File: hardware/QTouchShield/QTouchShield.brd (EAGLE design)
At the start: 100 x 80 mm, 114 parts, among them IC1 AT32UC3C0512CJEDEC-MS-026, U1 ARDUINO-MEGALITE

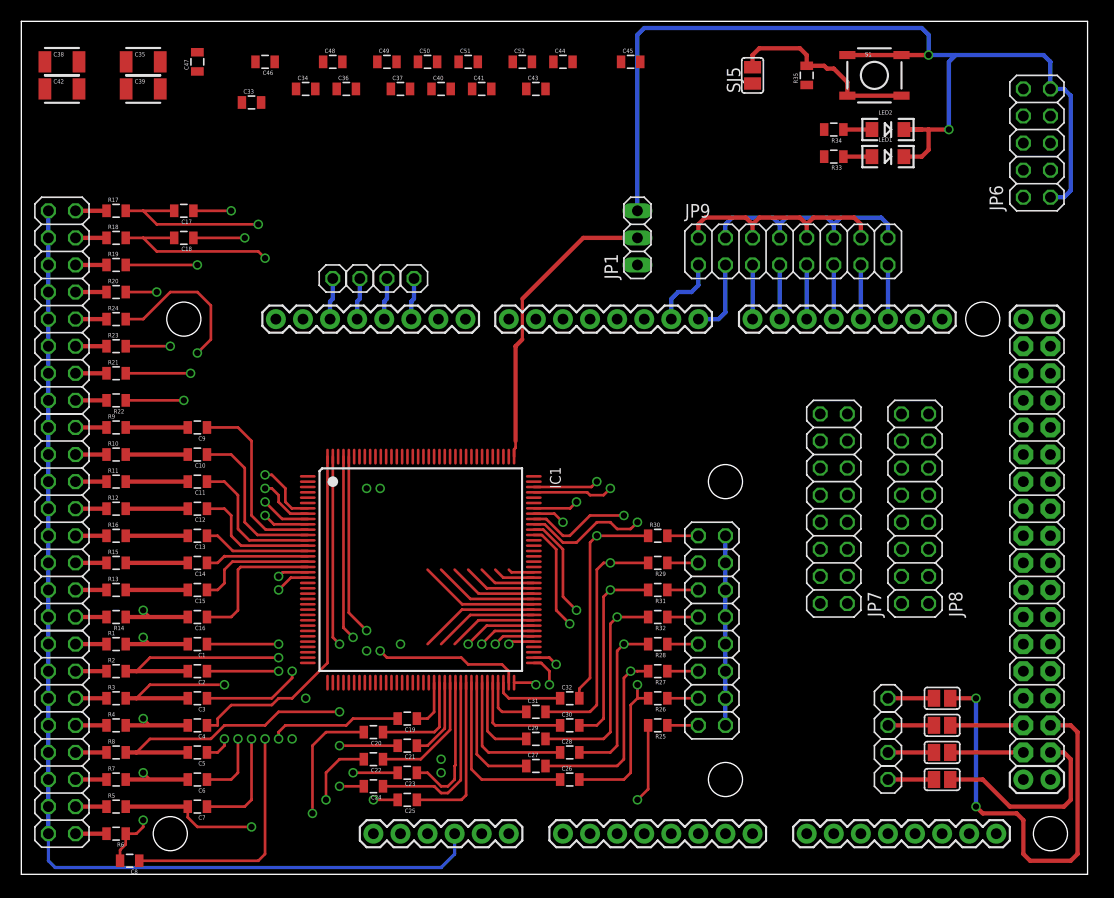
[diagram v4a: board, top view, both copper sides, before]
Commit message: Added cuttable bridges for RESET and SPI.
Added cuttable PCB bridges that allow default:
- RESET switch of shield connected to RESET of Arduino
- SPI interface selected as default interface
Defaults can be changed by cutting the bridges through with a scalpel.
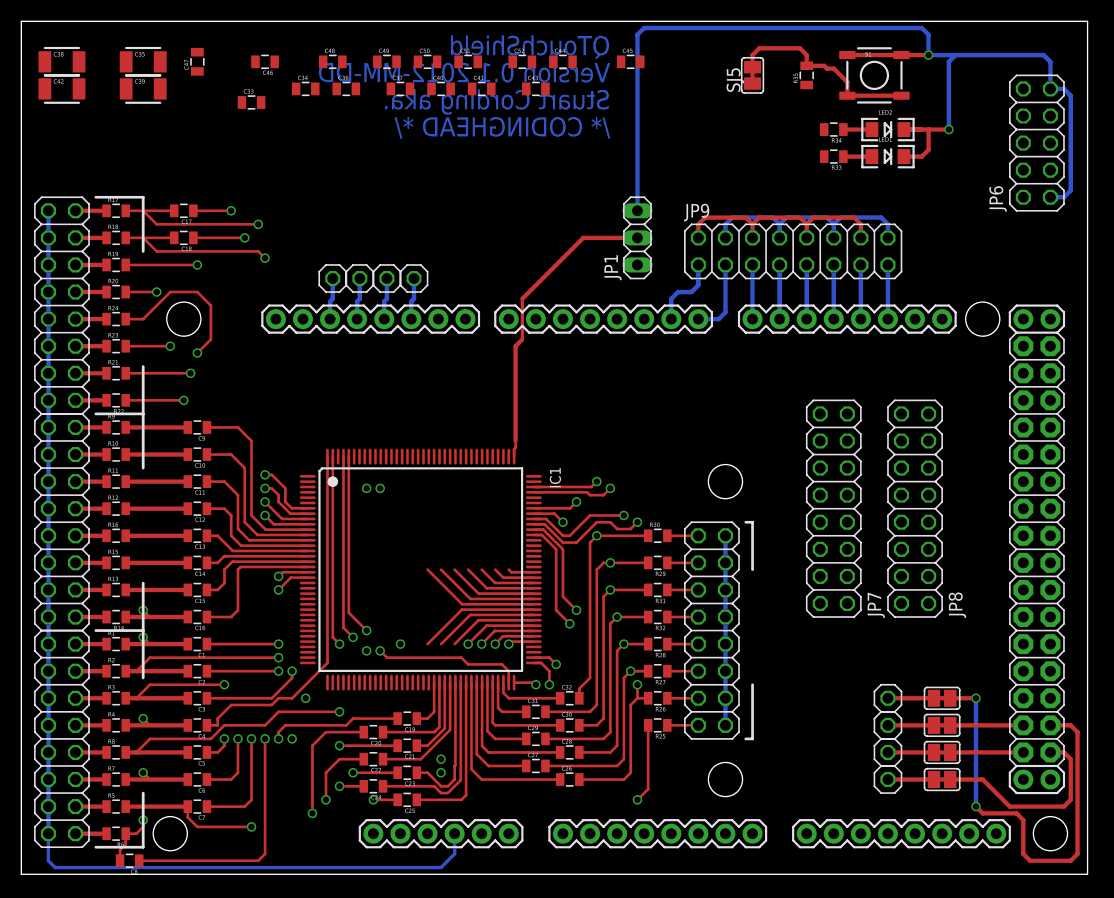
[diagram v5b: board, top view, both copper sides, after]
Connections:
- removed net MISO-PIN50: SJ4.1, U1.50
- removed net MOSI-PIN51: SJ3.1, U1.51
- removed net N$34: SJ5.1, U1.RESET
- removed net SCK-PIN52: SJ2.1, U1.52
- removed net SS-PIN53: SJ1.1, U1.53
- net JTAG_RESET: now also SJ5.1, U1.RESET
- net SDT-SPI0-MISO: now also SJ3.1, U1.51
- net SDT-SPI0-MOSI: now also SJ4.1, U1.50
- net SDT-SPI0-SCK: now also SJ2.1, U1.52
- net SDT-SPI0-SS: now also SJ1.1, U1.53
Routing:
- net SDT-SPI0-MISO: track 4.32 -> 46.4 mm, vias 0 -> 2
- net MOSI-PIN51: track 40.6 -> 0.00 mm, vias 2 -> 0
- net SDT-SPI0-SS: track 4.32 -> 24.4 mm
- net SS-PIN53: track 18.6 -> 0.00 mm
- net SDT-SPI0-SCK: track 4.32 -> 12.7 mm
- net SDT-SPI0-MOSI: track 4.32 -> 12.7 mm
- net SCK-PIN52: track 6.86 -> 0.00 mm
- net MISO-PIN50: track 6.86 -> 0.00 mm
- net JTAG_RESET: track 18.7 -> 20.3 mm
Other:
- board text added: "/* CODINGHEAD */"
- board text added: "QTouchShield"
- board text added: "Stuart Cording aka."
- board text added: "Version 0.1 2012-MM-DD"
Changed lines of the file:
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@@
 <wire x1="100" y1="80" x2="0" y2="80" width="0" layer="20"/>
 <wire x1="0" y1="80" x2="0" y2="0" width="0" layer="20"/>
+<wire x1="68.58" y1="28.575" x2="68.58" y2="33.02" width="0.254" layer="21"/>
+<wire x1="68.58" y1="33.02" x2="67.945" y2="33.02" width="0.254" layer="21"/>
+<wire x1="68.58" y1="17.78" x2="68.58" y2="12.7" width="0.254" layer="21"/>
+<wire x1="68.58" y1="12.7" x2="67.945" y2="12.7" width="0.254" layer="21"/>
+<wire x1="11.43" y1="58.42" x2="11.43" y2="63.5" width="0.254" layer="21"/>
+<wire x1="11.43" y1="63.5" x2="6.985" y2="63.5" width="0.254" layer="21"/>
+<wire x1="11.43" y1="47.625" x2="11.43" y2="43.18" width="0.254" layer="21"/>
+<wire x1="6.985" y1="43.18" x2="11.43" y2="43.18" width="0.254" layer="21"/>
+<wire x1="11.43" y1="43.18" x2="11.43" y2="38.1" width="0.254" layer="21"/>
+<wire x1="11.43" y1="27.305" x2="11.43" y2="22.86" width="0.254" layer="21"/>
+<wire x1="6.985" y1="22.86" x2="11.43" y2="22.86" width="0.254" layer="21"/>
+<wire x1="11.43" y1="22.86" x2="11.43" y2="18.415" width="0.254" layer="21"/>
+<wire x1="11.43" y1="7.62" x2="11.43" y2="2.54" width="0.254" layer="21"/>
+<wire x1="11.43" y1="2.54" x2="6.985" y2="2.54" width="0.254" layer="21"/>
+<text x="55.245" y="76.835" size="1.778" layer="16" font="vector" rot="MR0">QTouchShield</text>
+<text x="55.245" y="74.295" size="1.778" layer="16" font="vector" rot="MR0">Version 0.1 2012-MM-DD</text>
+<text x="55.245" y="71.755" size="1.778" layer="16" font="vector" rot="MR0">Stuart Cording aka.</text>
+<text x="55.245" y="69.215" size="1.778" layer="16" font="vector" rot="MR0">/* CODINGHEAD */</text>
 </plain>
 <attributes>
@@
 <wire x1="69.215" y1="77.47" x2="68.58" y2="76.835" width="0.4064" layer="1"/>
 <wire x1="68.58" y1="76.835" x2="68.58" y2="75.692" width="0.4064" layer="1"/>
+<contactref element="SJ5" pad="1"/>
+<contactref element="U1" pad="RESET"/>
 <wire x1="82.55" y1="73.025" x2="96.52" y2="68.58" width="0" layer="19" extent="1-1"/>
-<wire x1="29.715" y1="39.175" x2="68.58" y2="75.692" width="0" layer="19" extent="1-1"/>
+<wire x1="29.715" y1="39.175" x2="68.58" y2="74.168" width="0" layer="19" extent="1-1"/>
+<wire x1="33.02" y1="3.81" x2="29.715" y2="39.175" width="0" layer="19" extent="1-1"/>
+<wire x1="68.707" y1="75.565" x2="68.58" y2="75.565" width="0.4064" layer="1"/>
+<wire x1="68.58" y1="75.565" x2="68.58" y2="74.168" width="0.4064" layer="1"/>
 </signal>
 <signal name="N$1">
@@
 <contactref element="JP10" pad="1"/>
 <wire x1="81.28" y1="8.89" x2="85.598" y2="8.89" width="0.4064" layer="1"/>
-<wire x1="45.715" y1="39.175" x2="81.28" y2="8.89" width="0" layer="19" extent="1-1"/>
-</signal>
-<signal name="SDT-SPI0-MOSI">
-<contactref element="IC1" pad="111"/>
-<contactref element="SJ4" pad="2"/>
-<contactref element="JP13" pad="1"/>
-<wire x1="81.28" y1="13.97" x2="85.598" y2="13.97" width="0.4064" layer="1"/>
-<wire x1="45.215" y1="39.175" x2="81.28" y2="13.97" width="0" layer="19" extent="1-1"/>
-</signal>
-<signal name="SDT-SPI0-MISO">
-<contactref element="IC1" pad="112"/>
-<contactref element="SJ3" pad="2"/>
-<contactref element="JP12" pad="1"/>
-<wire x1="85.598" y1="16.51" x2="81.28" y2="16.51" width="0.4064" layer="1"/>
-<wire x1="44.715" y1="39.175" x2="81.28" y2="16.51" width="0" layer="19" extent="1-1"/>
-</signal>
-<signal name="SDT-SPI0-SCK">
-<contactref element="IC1" pad="113"/>
-<contactref element="SJ2" pad="2"/>
-<contactref element="JP11" pad="1"/>
-<wire x1="81.28" y1="11.43" x2="85.598" y2="11.43" width="0.4064" layer="1"/>
-<wire x1="44.215" y1="39.175" x2="81.28" y2="11.43" width="0" layer="19" extent="1-1"/>
-</signal>
-<signal name="SS-PIN53">
 <contactref element="U1" pad="53"/>
 <contactref element="SJ1" pad="1"/>
@@
 <wire x1="98.425" y1="10.795" x2="98.425" y2="6.985" width="0.4064" layer="1"/>
 <wire x1="98.425" y1="6.985" x2="97.79" y2="6.35" width="0.4064" layer="1"/>
-</signal>
-<signal name="SCK-PIN52">
-<contactref element="U1" pad="52"/>
-<contactref element="SJ2" pad="1"/>
-<wire x1="93.98" y1="11.43" x2="87.122" y2="11.43" width="0.4064" layer="1"/>
-</signal>
-<signal name="MOSI-PIN51">
+<wire x1="45.715" y1="39.175" x2="81.28" y2="8.89" width="0" layer="19" extent="1-1"/>
+<wire x1="85.598" y1="8.89" x2="87.122" y2="8.89" width="0.4064" layer="1"/>
+</signal>
+<signal name="SDT-SPI0-MOSI">
+<contactref element="IC1" pad="111"/>
+<contactref element="SJ4" pad="2"/>
+<contactref element="JP13" pad="1"/>
+<wire x1="81.28" y1="13.97" x2="85.598" y2="13.97" width="0.4064" layer="1"/>
+<contactref element="U1" pad="50"/>
+<contactref element="SJ4" pad="1"/>
+<wire x1="93.98" y1="13.97" x2="87.122" y2="13.97" width="0.4064" layer="1"/>
+<wire x1="45.215" y1="39.175" x2="81.28" y2="13.97" width="0" layer="19" extent="1-1"/>
+<wire x1="85.598" y1="13.97" x2="87.122" y2="13.97" width="0.4064" layer="1"/>
+</signal>
+<signal name="SDT-SPI0-MISO">
+<contactref element="IC1" pad="112"/>
+<contactref element="SJ3" pad="2"/>
+<contactref element="JP12" pad="1"/>
+<wire x1="85.598" y1="16.51" x2="81.28" y2="16.51" width="0.4064" layer="1"/>
 <contactref element="U1" pad="51"/>
 <contactref element="SJ3" pad="1"/>
@@
 <via x="89.535" y="16.51" extent="1-16" drill="0.6" shape="square"/>
 <wire x1="89.535" y1="16.51" x2="87.122" y2="16.51" width="0.4064" layer="1"/>
-</signal>
-<signal name="MISO-PIN50">
-<contactref element="U1" pad="50"/>
-<contactref element="SJ4" pad="1"/>
-<wire x1="93.98" y1="13.97" x2="87.122" y2="13.97" width="0.4064" layer="1"/>
+<wire x1="44.715" y1="39.175" x2="81.28" y2="16.51" width="0" layer="19" extent="1-1"/>
+<wire x1="85.598" y1="16.51" x2="87.122" y2="16.51" width="0.4064" layer="1"/>
+</signal>
+<signal name="SDT-SPI0-SCK">
+<contactref element="IC1" pad="113"/>
+<contactref element="SJ2" pad="2"/>
+<contactref element="JP11" pad="1"/>
+<wire x1="81.28" y1="11.43" x2="85.598" y2="11.43" width="0.4064" layer="1"/>
+<contactref element="U1" pad="52"/>
+<contactref element="SJ2" pad="1"/>
+<wire x1="93.98" y1="11.43" x2="87.122" y2="11.43" width="0.4064" layer="1"/>
+<wire x1="44.215" y1="39.175" x2="81.28" y2="11.43" width="0" layer="19" extent="1-1"/>
+<wire x1="85.598" y1="11.43" x2="87.122" y2="11.43" width="0.4064" layer="1"/>
 </signal>
 <signal name="ADCVREFP">
@@
 <wire x1="36.83" y1="53.975" x2="36.83" y2="55.88" width="0.4064" layer="16"/>
 </signal>
-<signal name="N$34">
-<contactref element="SJ5" pad="1"/>
-<contactref element="U1" pad="RESET"/>
-<wire x1="33.02" y1="3.81" x2="68.58" y2="74.168" width="0" layer="19" extent="1-1"/>
-</signal>
 </signals>
